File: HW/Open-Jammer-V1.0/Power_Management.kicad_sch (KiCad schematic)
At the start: 14 parts, among them J1 S2B-PH-SM4-TB(LF)(SN), U1 MCP73831, U2 DW01, U3 FS8205A, U4 LM66200DRLR

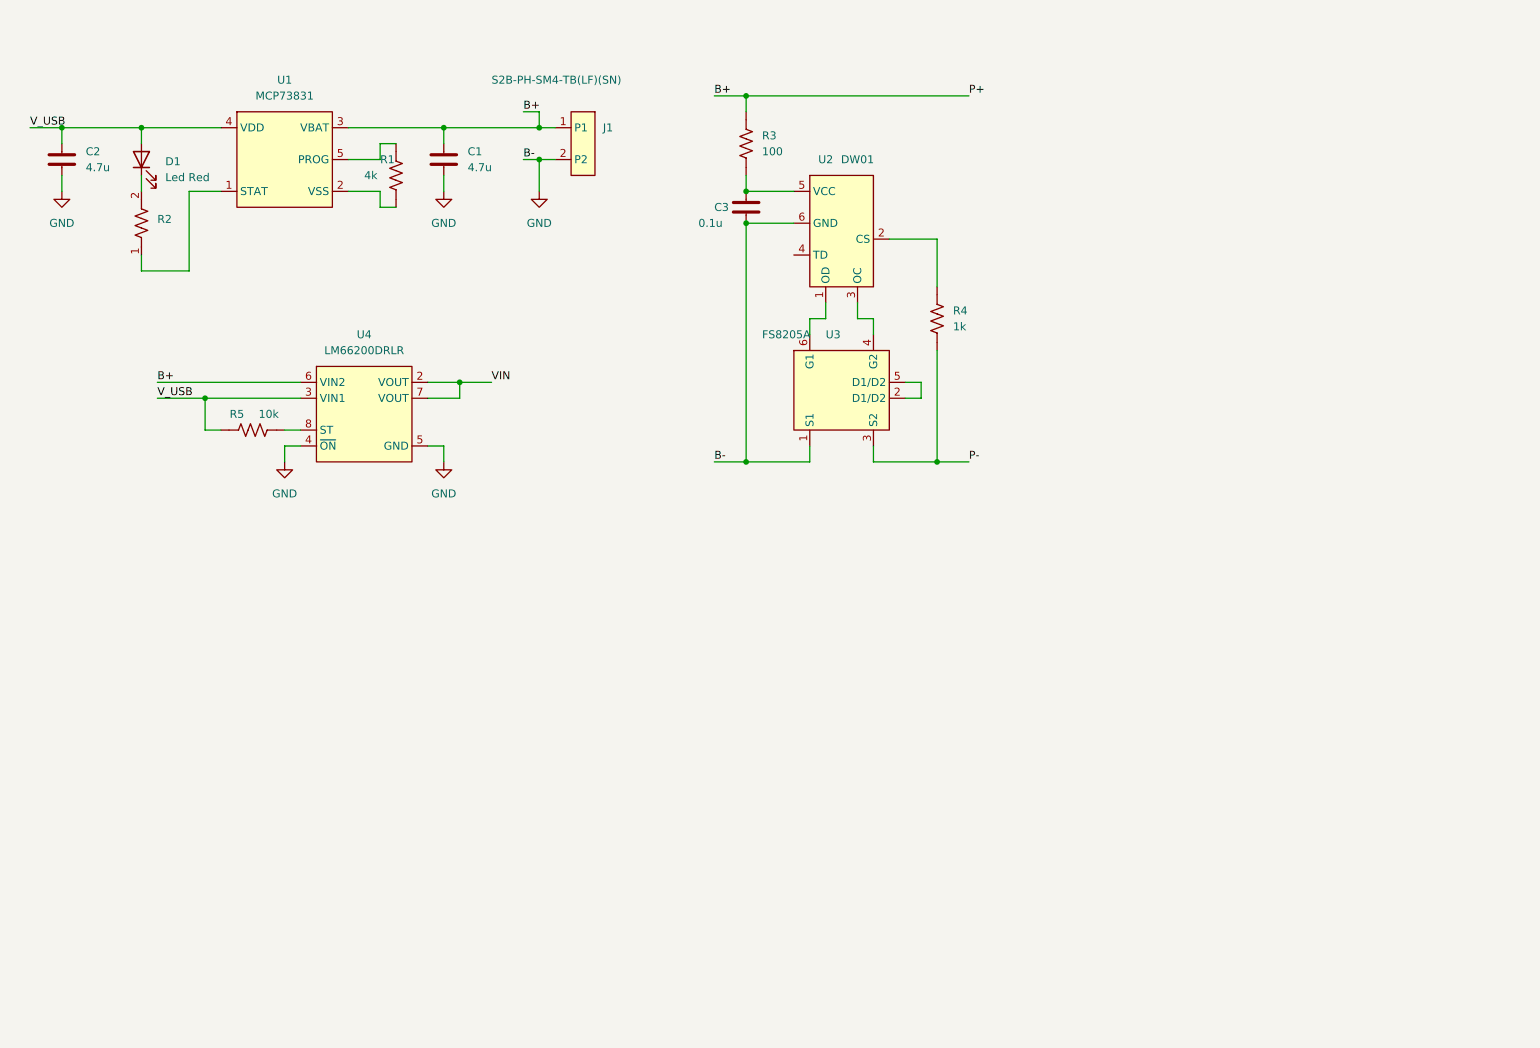
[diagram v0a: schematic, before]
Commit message: advances in schematics
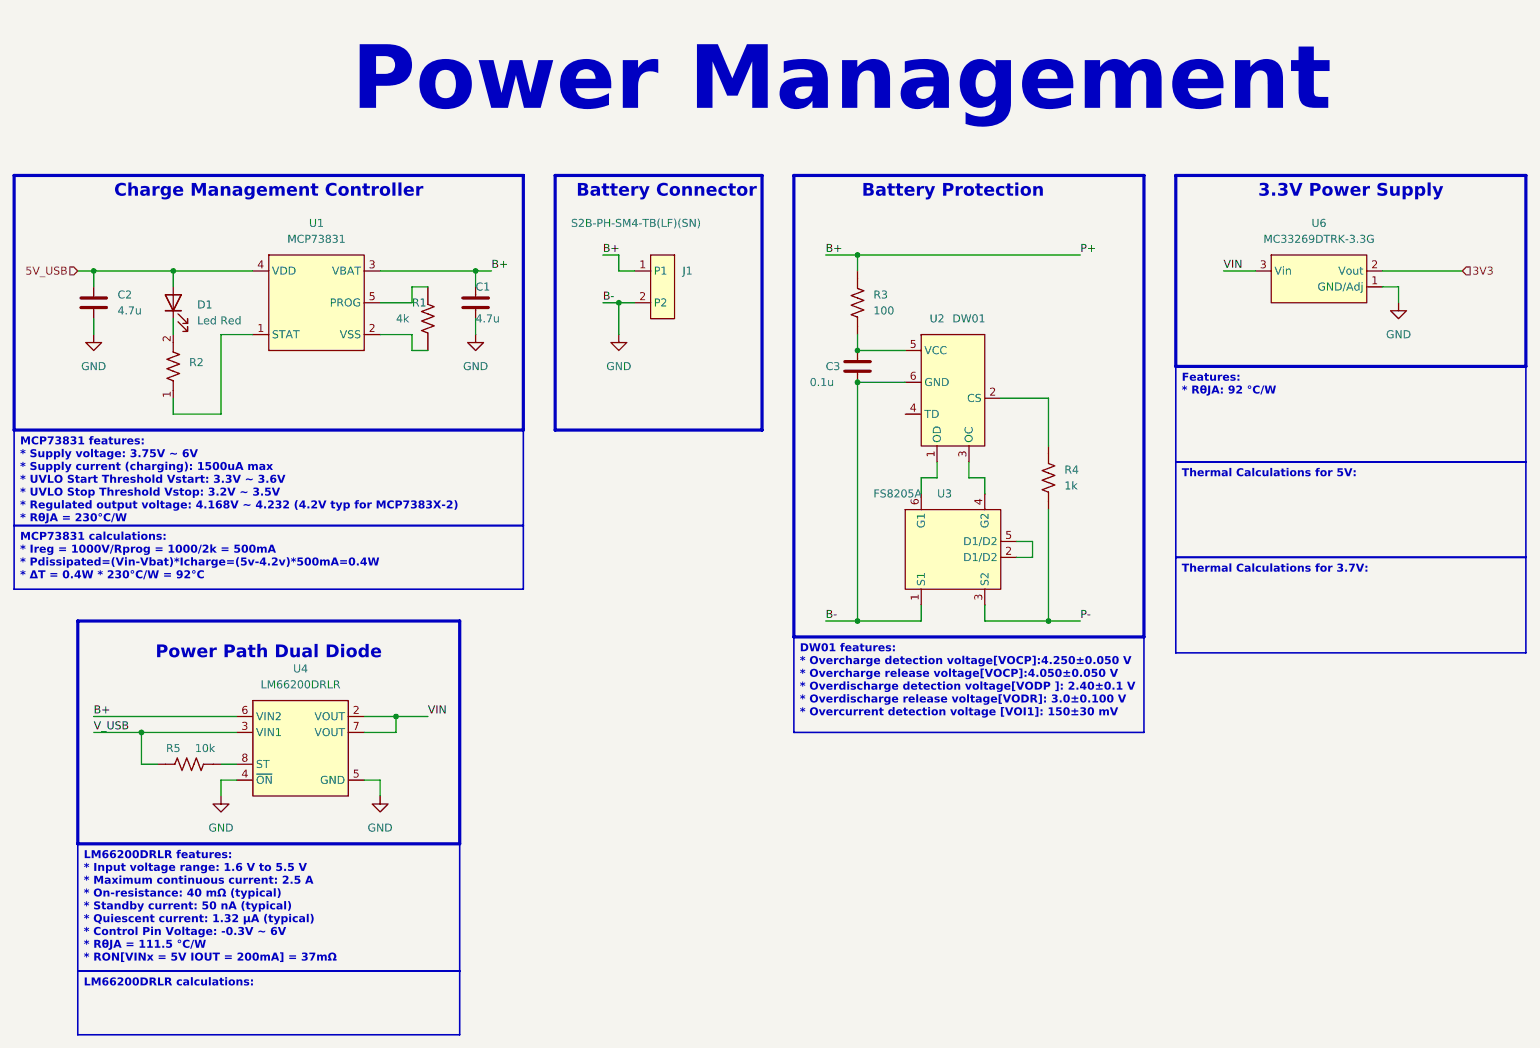
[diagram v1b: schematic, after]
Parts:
- added U6: MC33269DTRK-3.3G, symbol Open-Jammer:MC33269DTRK-3.3G
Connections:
- net GND: now also U6.1 (GND/Adj)
- net VIN: now also U6.3 (Vin)
- net V_USB: no longer C2.2, D1.2 (A), U1.4 (VDD)
- new net 3V3: U6.2 (Vout)
- new net 5V_USB: C2.2, D1.2 (A), U1.4 (VDD)
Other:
- note added: "3.3V Power Supply"
- note added: "Battery Connector"
- note added: "Battery Protection"
- note added: "Charge Management Controller"
- note added: "Power Management"
- note added: "Power Path Dual Diode"
- moved on the sheet: C1, C2, C3, D1, J1, R1, R2, R3, R4, R5, U1, U2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

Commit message: Added reset and boot buttons. Added oled screen. Added ESP32 VCC capacitors
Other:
- title: (none) -> Oper Jammer V1R0
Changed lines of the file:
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@@
 	(generator_version "9.0")
 	(paper "A4")
+	(title_block
+		(title "Oper Jammer V1R0")
+		(rev "V1R0")
+	)
 	(rectangle
 		(start 20.32 40.64)
